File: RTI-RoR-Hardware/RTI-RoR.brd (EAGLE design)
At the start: 80 x 71.1 mm, 30 parts, among them IC2 74LVC244

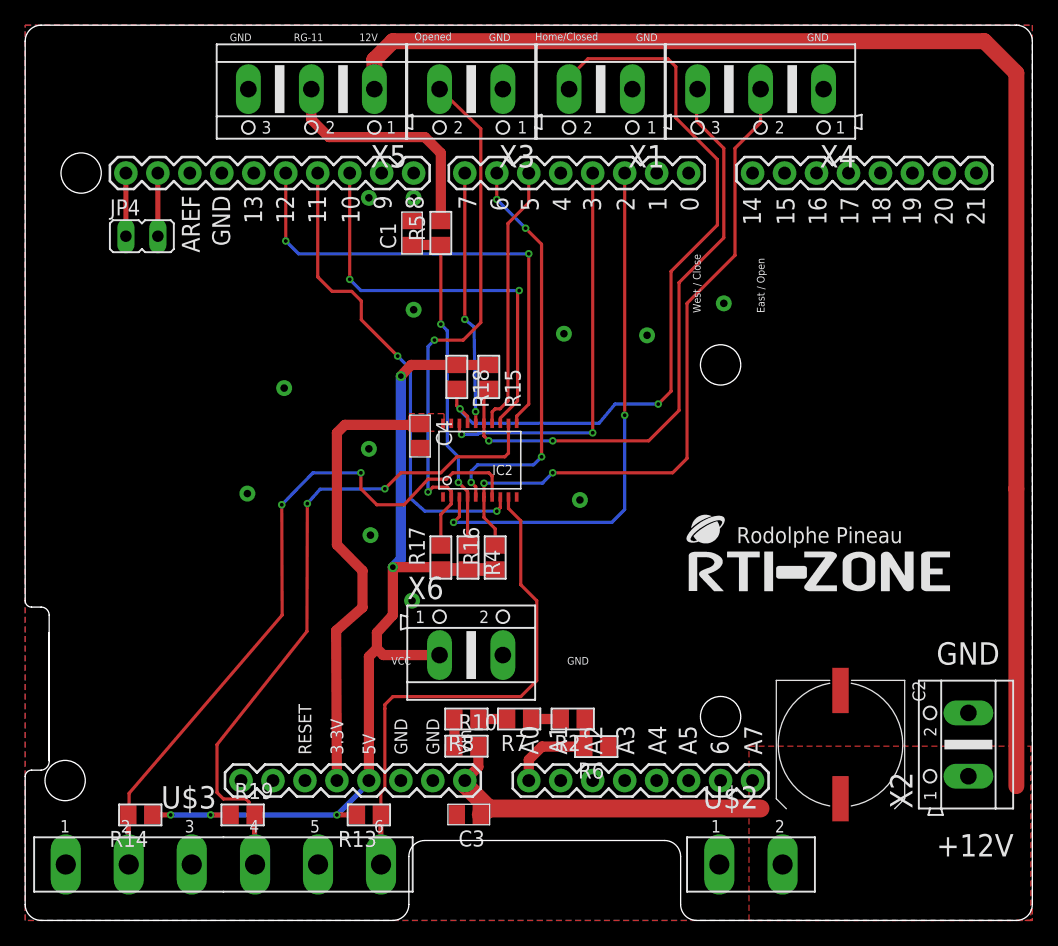
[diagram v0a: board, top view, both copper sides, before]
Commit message: Adding the at park pins to both PCB for the Arduino DUE.
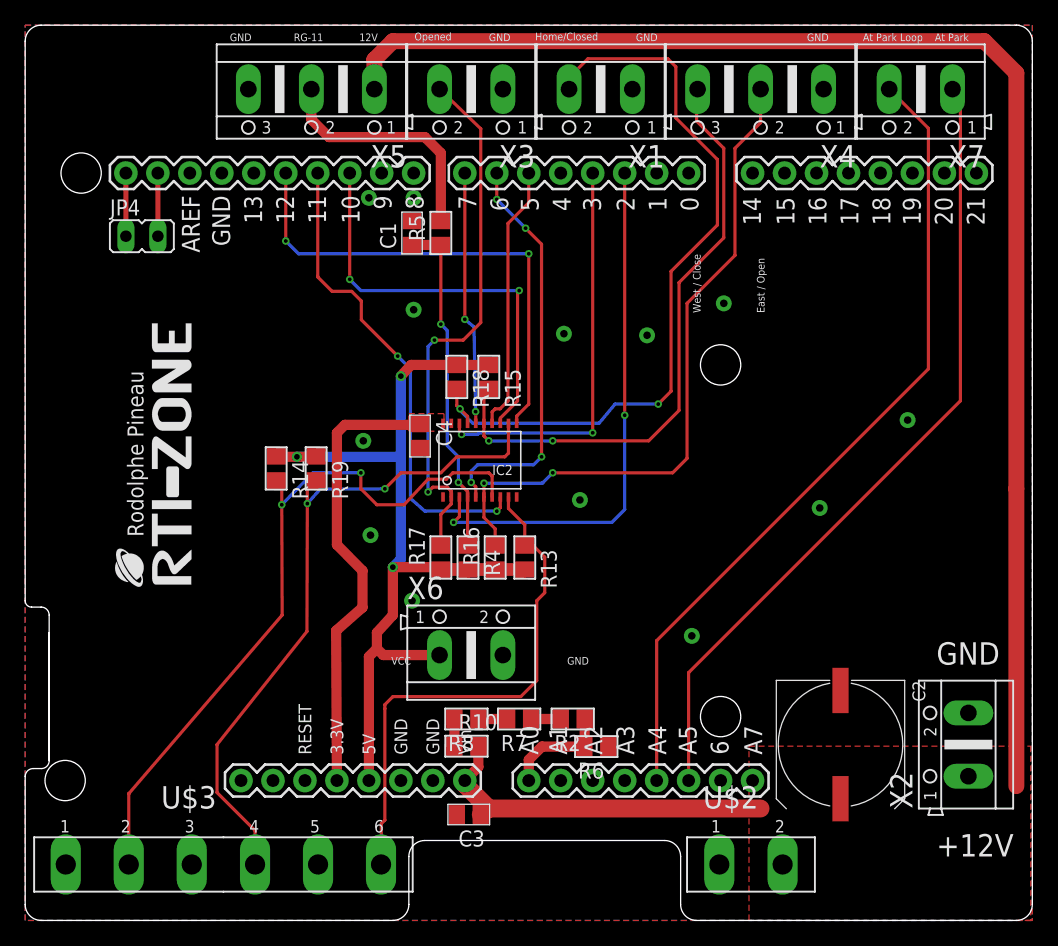
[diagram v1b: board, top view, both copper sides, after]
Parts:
- added X7: (no value), con-ptr500:AK500/2
- moved U$4 39.5 mm to (13.2, 26.7), turned to 90 degrees
- moved R14 29.6 mm to (19.9, 35.9), turned to 270 degrees
- moved R19 28.1 mm to (23.1, 35.9), turned to 270 degrees
- moved R13 23.9 mm to (39.7, 28.8), turned to 270 degrees
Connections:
- new net AT_PARK_PIN: PCB1.A5, X7.1
- new net AT_PARK_PIN_LOOP: PCB1.A4, X7.2
- new net XBEE_RESET: PCB1.8
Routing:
- net AT_PARK_PIN_LOOP: track 0.00 -> 65.2 mm
- net AT_PARK_PIN: track 0.00 -> 64.1 mm
- net VCC: track 75.5 -> 67.7 mm, vias 5 -> 3
- net M_EN_5V: track 55.6 -> 57.6 mm
- net M_DIR_5V: track 53.5 -> 54.6 mm
- net M_STEP_5V: track 41.2 -> 42.1 mm
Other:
- outline, holes or cut-outs redrawn
- board text added: "At Park"
- board text added: "At Park Loop"
